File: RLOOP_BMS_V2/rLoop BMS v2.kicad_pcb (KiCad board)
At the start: 2 copper layers, 79 x 133 mm, 423 parts, among them J1 1241050-7, J2 2-640387-0, J3 TE 2-292161-3, Q1 VOS618A-2X001T, Q10 PMV20ENR, Q11 PMV20ENR, Q12 PMV20ENR, Q13 PMV20ENR, Q14 PMV20ENR, Q15 PMV20ENR, Q16 PMV20ENR, Q17 PMV20ENR, Q18 PMV20ENR, Q19 PMV20ENR, Q2 PMV20ENR, Q3 PMV20ENR, Q4 PMV20ENR, Q5 PMV20ENR, Q6 PMV20ENR, Q7 PMV20ENR, Q8 PMV20ENR, Q9 PMV20ENR, U1 bq76PL536A_HTQFP, U2 bq76PL536A_HTQFP, U3 bq76PL536A_HTQFP, U4 MIC5282-5.0YMM, U5 VOS618A-2X001T

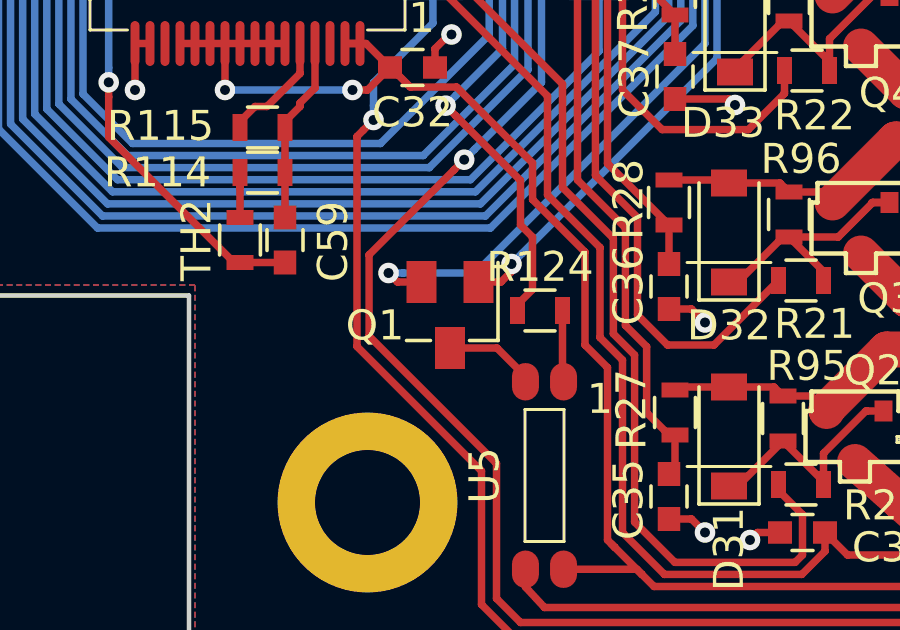
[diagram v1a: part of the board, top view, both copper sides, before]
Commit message: change Q1 transistor
Fixing something out of stock
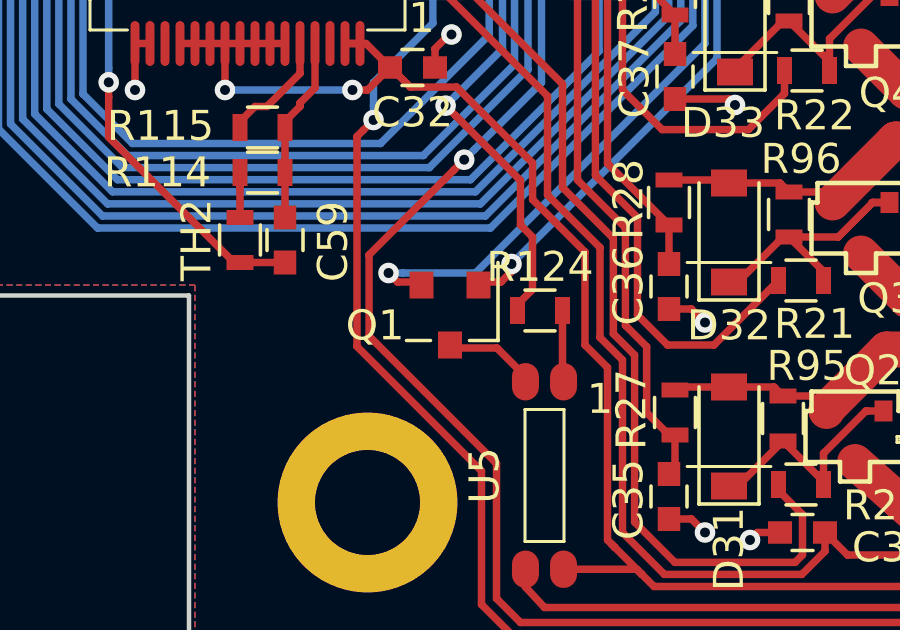
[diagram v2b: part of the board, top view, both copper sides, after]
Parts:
- Q1: footprint TO_SOT_Packages_SMD:SuperSOT-3 -> rLoop_Footprints:SOT-23
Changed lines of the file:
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@@
     )
   )
-  (module TO_SOT_Packages_SMD:SuperSOT-3 (layer F.Cu)
-    (at 64.5 164.75 270)
-    (descr "3-pin SuperSOT package https://www.fairchildsemi.com/package-drawings/MA/MA03B.pdf")
-    (tags "SuperSOT-3 SSOT-3")
-    (attr smd)
-    (fp_text reference Q1 (at 0.35 2.5 360) (layer F.SilkS)
-      (effects (font (size 1 1) (thickness 0.15)))
-    )
-    (fp_text value VOS618A-2X001T (at 0 2.4 270) (layer F.Fab)
-      (effects (font (size 1 1) (thickness 0.15)))
-    )
-    (fp_text user %R (at -2.75 0 360) (layer F.Fab)
-      (effects (font (size 0.5 0.5) (thickness 0.075)))
-    )
-    (fp_line (start 0.85 0.65) (end 0.85 1.45) (layer F.SilkS) (width 0.12))
-    (fp_line (start -1.75 -1.6) (end 0.85 -1.6) (layer F.SilkS) (width 0.12))
-    (fp_line (start 0.85 -1.6) (end 0.85 -0.65) (layer F.SilkS) (width 0.12))
-    (fp_line (start 0.7 -1.45) (end 0.7 1.45) (layer F.Fab) (width 0.12))
-    (fp_line (start 0.7 1.45) (end -0.7 1.45) (layer F.Fab) (width 0.12))
-    (fp_line (start -0.7 1.45) (end -0.7 -0.9) (layer F.Fab) (width 0.12))
-    (fp_line (start -0.7 -0.9) (end -0.15 -1.45) (layer F.Fab) (width 0.12))
-    (fp_line (start -0.15 -1.45) (end 0.7 -1.45) (layer F.Fab) (width 0.12))
-    (fp_line (start -2.05 -1.7) (end 2.05 -1.7) (layer F.CrtYd) (width 0.05))
-    (fp_line (start -2.05 -1.7) (end -2.05 1.7) (layer F.CrtYd) (width 0.05))
-    (fp_line (start 2.05 1.7) (end 2.05 -1.7) (layer F.CrtYd) (width 0.05))
-    (fp_line (start 2.05 1.7) (end -2.05 1.7) (layer F.CrtYd) (width 0.05))
-    (pad 1 smd rect (at -1.1 -0.95 270) (size 1.4 1) (layers F.Cu F.Paste F.Mask)
-      (net 218 "/ISO POWER/COMMS_EN"))
-    (pad 2 smd rect (at -1.1 0.95 270) (size 1.4 1) (layers F.Cu F.Paste F.Mask)
-      (net 45 MCU_GND))
-    (pad 3 smd rect (at 1.1 0 270) (size 1.4 1) (layers F.Cu F.Paste F.Mask)
-      (net 219 "Net-(Q1-Pad3)"))
-    (model ${KISYS3DMOD}/TO_SOT_Packages_SMD.3dshapes/SuperSOT-3.wrl
-      (at (xyz 0 0 0))
-      (scale (xyz 1 1 1))
-      (rotate (xyz 0 0 0))
-    )
-  )
   (module Resistors_SMD:R_0603 (layer F.Cu)
     (at 67.5 164.6)
@@
       (at (xyz 0 0 0))
       (scale (xyz 1 1 1))
+      (rotate (xyz 0 0 0))
+    )
+  )
+  (module rLoop_Footprints:SOT-23 (layer F.Cu)
+    (at 64.5 164.75 270)
+    (descr "3-pin SuperSOT package https://www.fairchildsemi.com/package-drawings/MA/MA03B.pdf")
+    (tags "SuperSOT-3 SSOT-3")
+    (attr smd)
+    (fp_text reference Q1 (at 0.35 2.5 360) (layer F.SilkS)
+      (effects (font (size 1 1) (thickness 0.15)))
+    )
+    (fp_text value VOS618A-2X001T (at 0 2.4 270) (layer F.Fab)
+      (effects (font (size 1 1) (thickness 0.15)))
+    )
+    (fp_text user %R (at -2.75 0 360) (layer F.Fab)
+      (effects (font (size 0.5 0.5) (thickness 0.075)))
+    )
+    (fp_line (start 0.85 0.65) (end 0.85 1.45) (layer F.SilkS) (width 0.12))
+    (fp_line (start -1.75 -1.6) (end 0.85 -1.6) (layer F.SilkS) (width 0.12))
+    (fp_line (start 0.85 -1.6) (end 0.85 -0.65) (layer F.SilkS) (width 0.12))
+    (fp_line (start 0.7 -1.45) (end 0.7 1.45) (layer F.Fab) (width 0.12))
+    (fp_line (start 0.7 1.45) (end -0.7 1.45) (layer F.Fab) (width 0.12))
+    (fp_line (start -0.7 1.45) (end -0.7 -0.9) (layer F.Fab) (width 0.12))
+    (fp_line (start -0.7 -0.9) (end -0.15 -1.45) (layer F.Fab) (width 0.12))
+    (fp_line (start -0.15 -1.45) (end 0.7 -1.45) (layer F.Fab) (width 0.12))
+    (fp_line (start -2.05 -1.7) (end 2.05 -1.7) (layer F.CrtYd) (width 0.05))
+    (fp_line (start -2.05 -1.7) (end -2.05 1.7) (layer F.CrtYd) (width 0.05))
+    (fp_line (start 2.05 1.7) (end 2.05 -1.7) (layer F.CrtYd) (width 0.05))
+    (fp_line (start 2.05 1.7) (end -2.05 1.7) (layer F.CrtYd) (width 0.05))
+    (pad 1 smd rect (at -1 -0.95 270) (size 0.9 0.8) (layers F.Cu F.Paste F.Mask)
+      (net 218 "/ISO POWER/COMMS_EN"))
+    (pad 2 smd rect (at -1 0.95 270) (size 0.9 0.8) (layers F.Cu F.Paste F.Mask)
+      (net 45 MCU_GND))
+    (pad 3 smd rect (at 1 0 270) (size 0.9 0.8) (layers F.Cu F.Paste F.Mask)
+      (net 219 "Net-(Q1-Pad3)"))
+    (model ${KISYS3DMOD}/TO_SOT_Packages_SMD.3dshapes/SuperSOT-3.wrl
+      (at (xyz 0 0 0))
+      (scale (xyz 1 1 1))

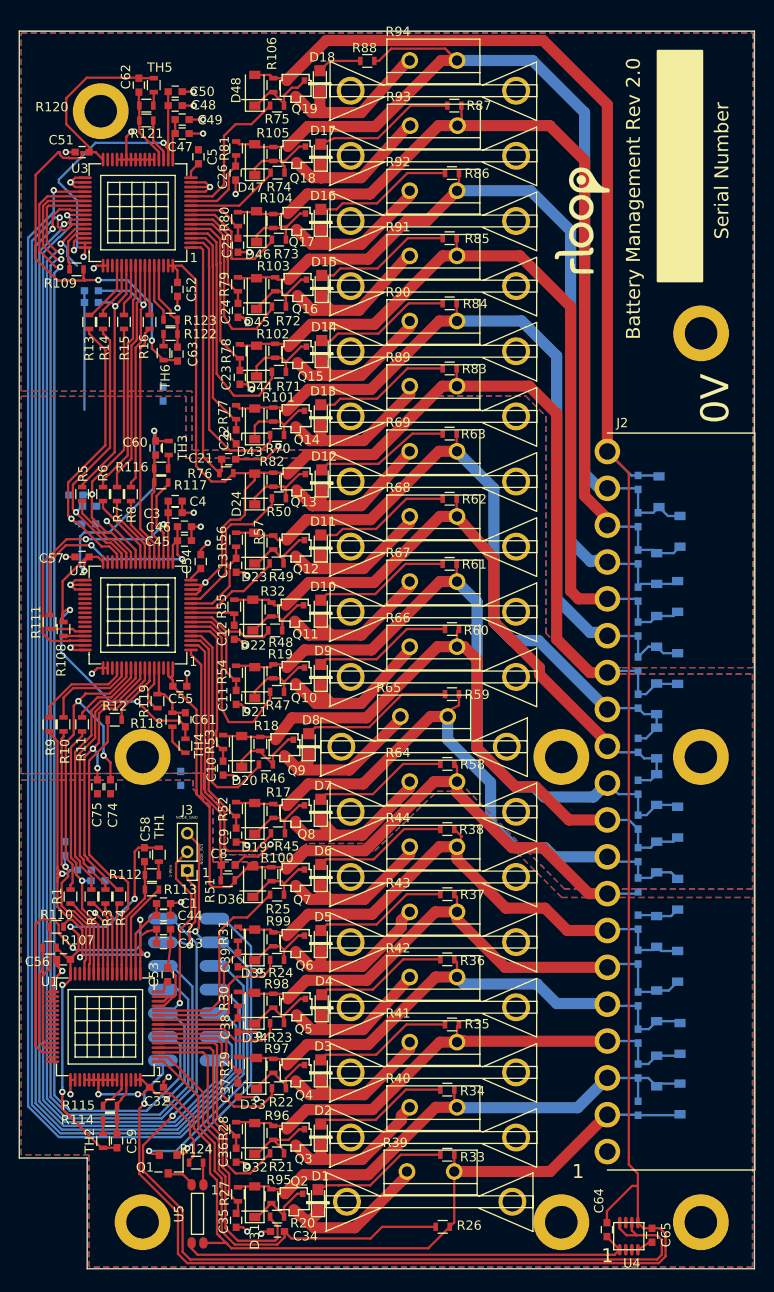
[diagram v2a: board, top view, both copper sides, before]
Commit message: swapped a few connectors to standardize with the power node and what's readily available
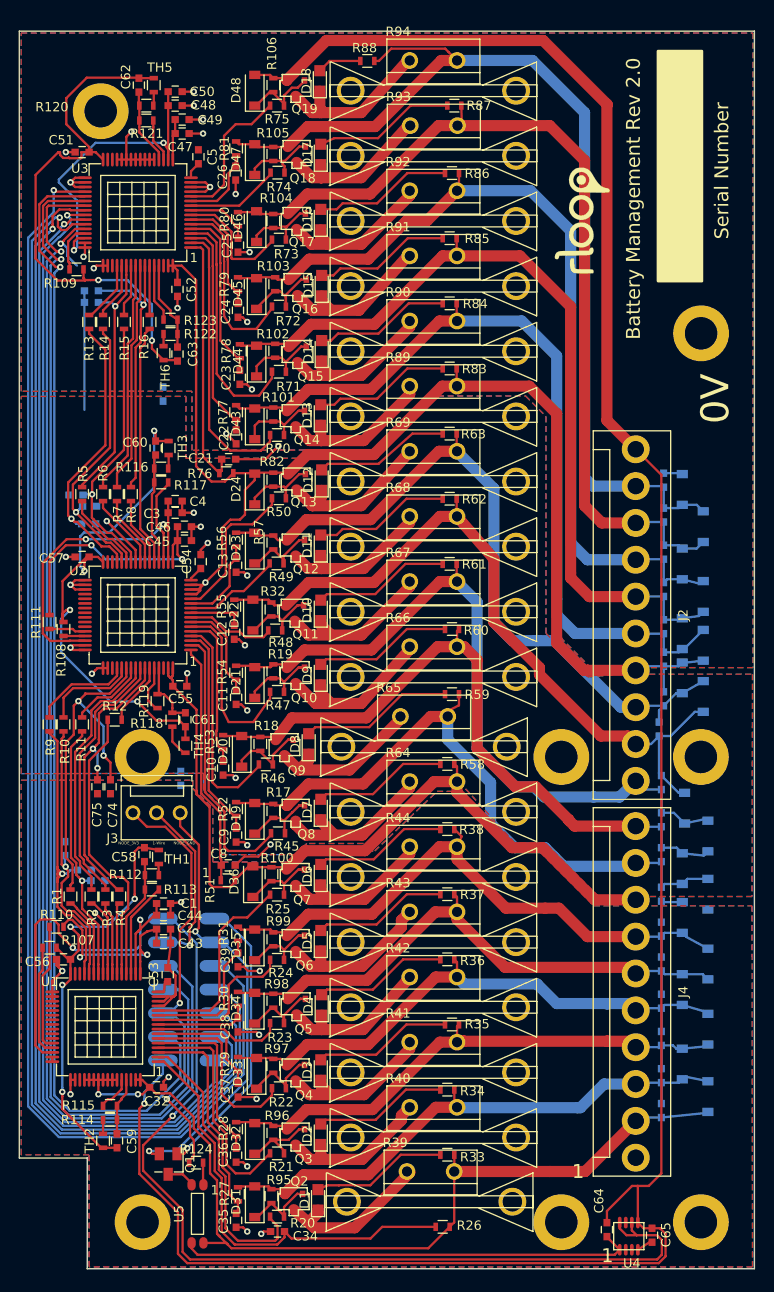
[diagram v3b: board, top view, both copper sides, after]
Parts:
- added J4: 1-640445-0, rLoop_Footprints:1-640445-0, F.Cu at (114.8, 146.2)
- D1, D10, D11, D12, D13, D14, D15, D16, D17, D18, D2, D3, D4, D5, D6, D7, D8, D9: footprint rLoop_Footprints:LED_0805 -> LEDs:LED_0805
- D19, D20, D21, D22, D23, D24, D25, D26, D27, D28, D29, D30, D43, D44, D45, D46, D47, D48, D49, D50, D51, D52, D53, D54: value 5.1 V / SOD-123 -> SMF6.5A / SOD-123; footprint rLoop_Footprints:D_SOD-123 -> Diodes_SMD:D_SOD-123
- D31, D32, D33, D34, D35, D36, D37, D38, D39, D40, D41, D42: value 5.1 VDC / SOD-123 -> SMF6.5A / SOD-123; footprint rLoop_Footprints:D_SOD-123 -> Diodes_SMD:D_SOD-123
- J2: value 2-640387-0 -> 1-640445-0; footprint rLoop_Footprints:TE_2-640387-0 -> rLoop_Footprints:1-640445-0
- J3: value TE 2-292161-3 -> TE 3-641215-3; footprint Pin_Headers:Pin_Header_Straight_1x03_Pitch2.00mm -> rLoop_Footprints:3-641215-3_3Pin_Latching_Header
- Q1: value VOS618A-2X001T -> NTR4170N; footprint rLoop_Footprints:SOT-23 -> TO_SOT_Packages_SMD:SuperSOT-3
- R39, R40, R41, R42, R43, R44, R89, R90, R91, R92, R93, R94: value MP930-2.00-1% -> TBH25P2R00JE
- moved J2 20.3 mm to (114.8, 105.8), turned to 90 degrees
- moved D29 7.07 mm to (122.0, 114.5)
- moved J3 7.02 mm to (63.2, 127.0), turned to 0 degrees
- moved D49 3.72 mm to (122.0, 109.0)
- moved D28 3.61 mm to (120.0, 126.5)
- moved D27 3.58 mm to (122.5, 129.5)
- moved D30 3.55 mm to (119.8, 112.5)
- moved D40 3.26 mm to (119.8, 146.0)
- moved D41 3.26 mm to (122.5, 143.2)
- moved D25 3.25 mm to (122.5, 135.8)
- moved D39 3.16 mm to (122.5, 150.2)
- moved D42 3.13 mm to (119.8, 138.2)
- moved D26 3.02 mm to (119.8, 133.0)
- moved D37 3.01 mm to (122.5, 157.5)
- moved C16 2.85 mm to (117.2, 118.0)
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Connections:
- J2 pad 1: Net-(J2-Pad1) -> GND_1
- J2 pad 10: /DISCHARGE_2/CELL_4 -> /DISCHARGE_2/CELL_3
- J2 pad 2: VDDHV_3 -> /DISCHARGE_1/CELL_1
- J2 pad 3: /DISCHARGE_3/CELL_5 -> /DISCHARGE_1/CELL_2
- J2 pad 4: /DISCHARGE_3/CELL_4 -> /DISCHARGE_1/CELL_3
- J2 pad 5: /DISCHARGE_3/CELL_3 -> /DISCHARGE_1/CELL_4
- J2 pad 6: /DISCHARGE_3/CELL_2 -> /DISCHARGE_1/CELL_5
- J2 pad 7: /DISCHARGE_3/CELL_1 -> GND_2
- J2 pad 8: GND_3 -> /DISCHARGE_2/CELL_1
- J2 pad 9: /DISCHARGE_2/CELL_5 -> /DISCHARGE_2/CELL_2
- J3 pad 1: Net-(J1-Pad12) -> MCU_GND
- J3 pad 2: MCU_3V3 -> Net-(J1-Pad12)
- J3 pad 3: MCU_GND -> MCU_3V3
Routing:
- net /DISCHARGE_2/CELL_2: track 71.1 -> 80.8 mm
- net Net-(J1-Pad12): track 11.6 -> 19.1 mm
- net MCU_3V3: track 40.0 -> 46.8 mm
- net /DISCHARGE_2/CELL_3: track 76.5 -> 81.2 mm
- net /DISCHARGE_2/CELL_5: track 67.5 -> 72.0 mm
- net /DISCHARGE_3/CELL_1: track 61.1 -> 65.4 mm
- net /DISCHARGE_2/CELL_1: track 75.7 -> 79.8 mm
- net /DISCHARGE_1/CELL_5: track 85.7 -> 89.7 mm
- net /DISCHARGE_3/CELL_4: track 56.7 -> 60.3 mm
- net /DISCHARGE_3/CELL_3: track 58.1 -> 61.7 mm
- net GND_2: track 185.1 -> 188.4 mm
- net /DISCHARGE_2/CELL_4: track 71.8 -> 75.0 mm
- net /DISCHARGE_1/CELL_3: track 92.1 -> 95.3 mm
- net VDDHV_3: track 98.4 -> 101.4 mm
- net /DISCHARGE_3/CELL_2: track 60.2 -> 63.1 mm
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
